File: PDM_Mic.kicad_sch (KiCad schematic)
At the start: 25 parts, among them J4 Conn_FFC_Molex_5019510550, J5 Conn_FFC_Molex_5019510550, U18 TPD4E05U06QDQARQ1, U19 TPD4E05U06QDQARQ1, U20 TLV73318PDBVT, U21 ADAU7118ACPZRL

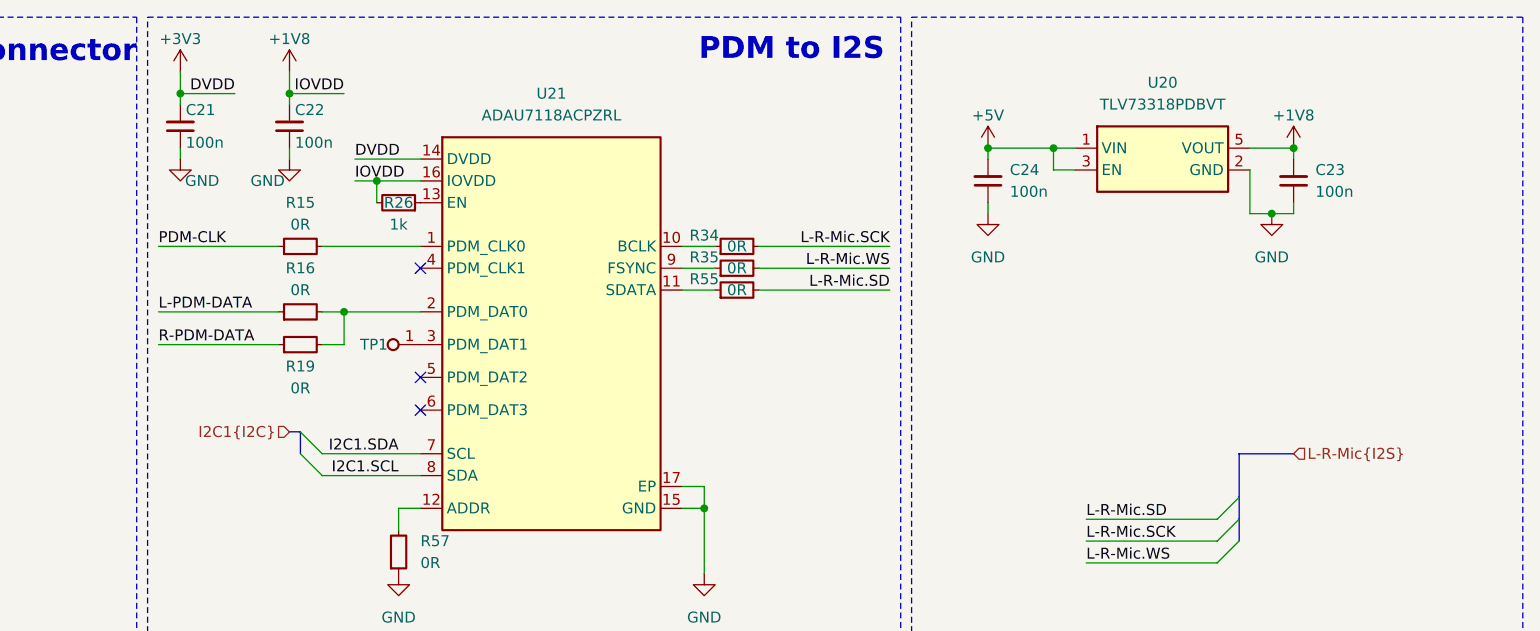
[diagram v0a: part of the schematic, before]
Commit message: [#71230] Route I2S and PDM
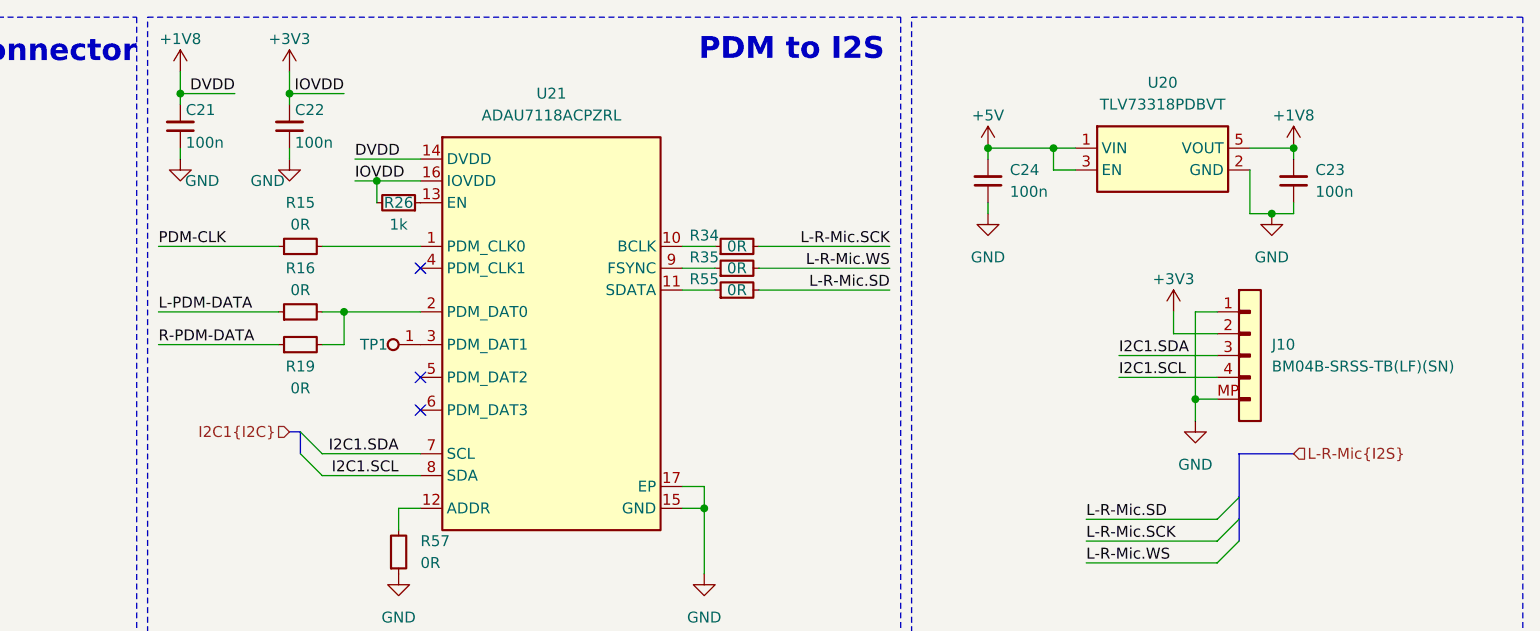
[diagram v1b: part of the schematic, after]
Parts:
- added J10: JST_SH_1x4_BM04B-SRSS-TB-LF-SN, antmicro-footprints:Conn_JST_SH_1x4_BM04B-SRSS-TB-LF-SN, symbol antmicroWire2BoardConnectors:JST_SH_1x4_BM04B-SRSS-TB-LF-SN
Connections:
- net +1V8: now also C21.2, U21.14 (DVDD); no longer C22.2, R26.2, U21.16 (IOVDD)
- net +3V3: now also C22.2, R26.2, U21.16 (IOVDD), J10.2; no longer C21.2, U21.14 (DVDD)
- net GND: now also J10.1, J10.MP
- net I2C1.SCL: now also J10.4
- net I2C1.SDA: now also J10.3

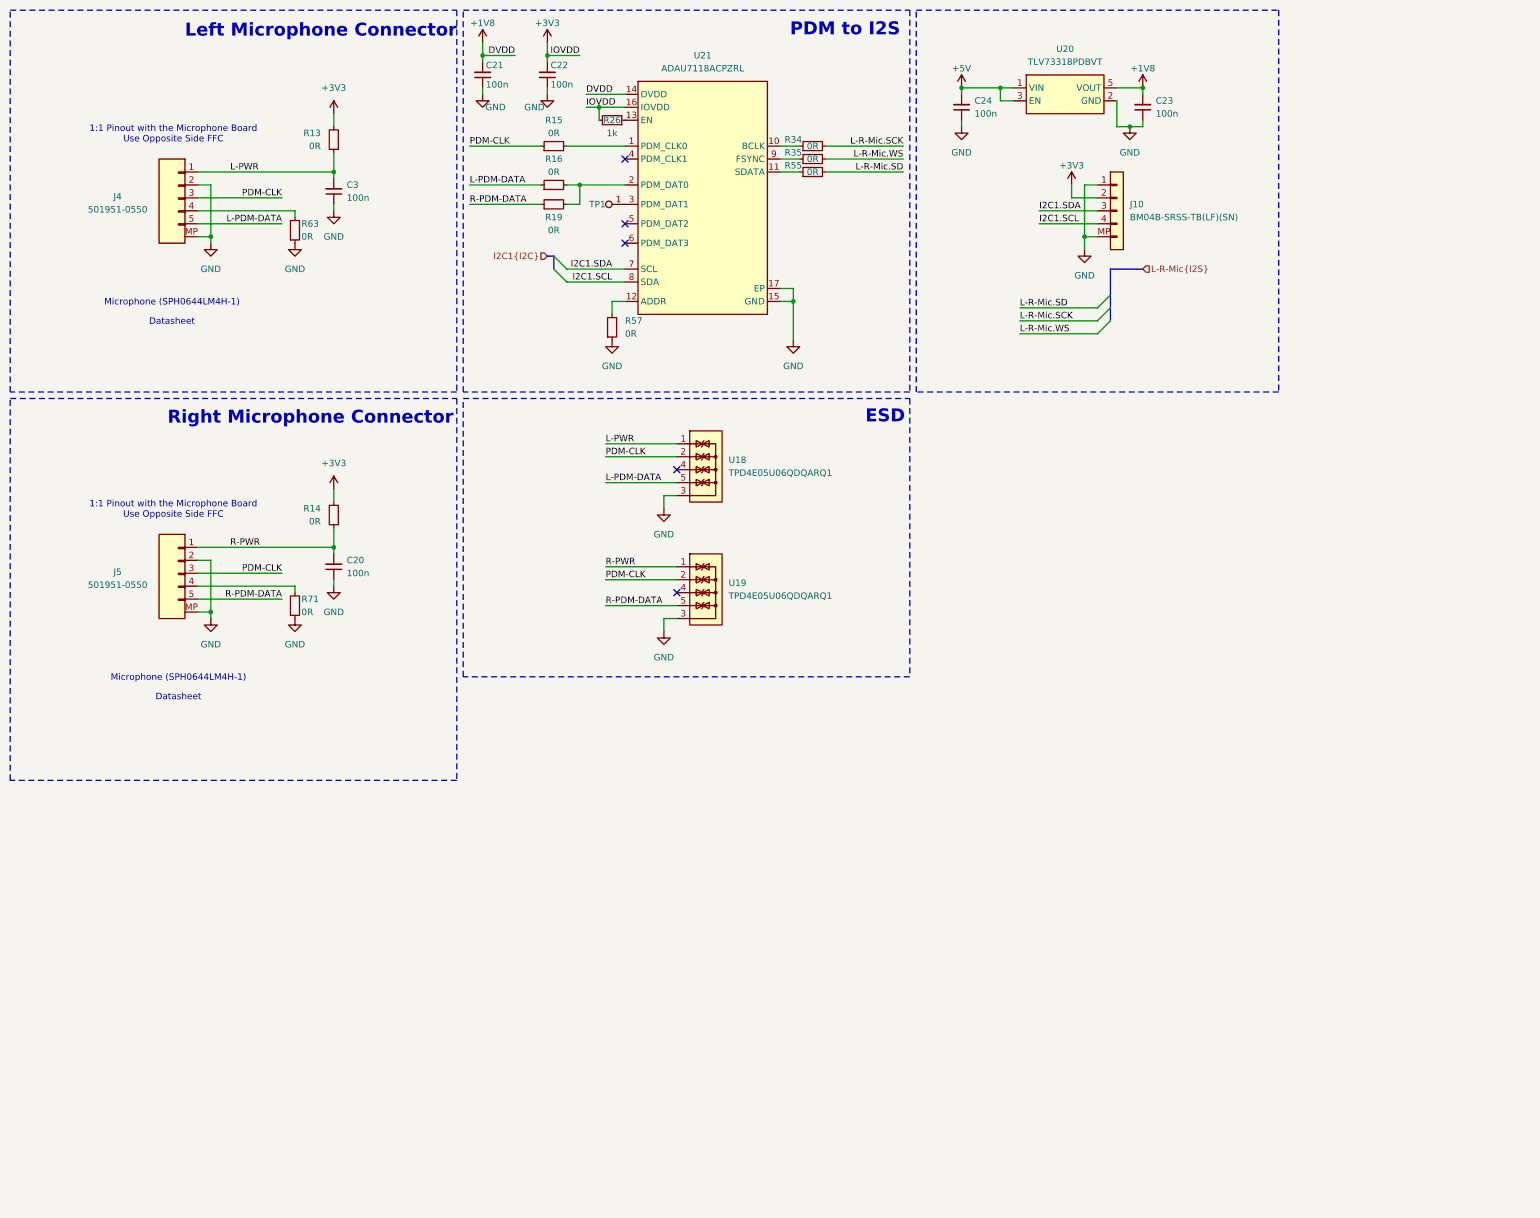
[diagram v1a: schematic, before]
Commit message: [#71230] Add option to connect PDM mic directly to RP2040-0
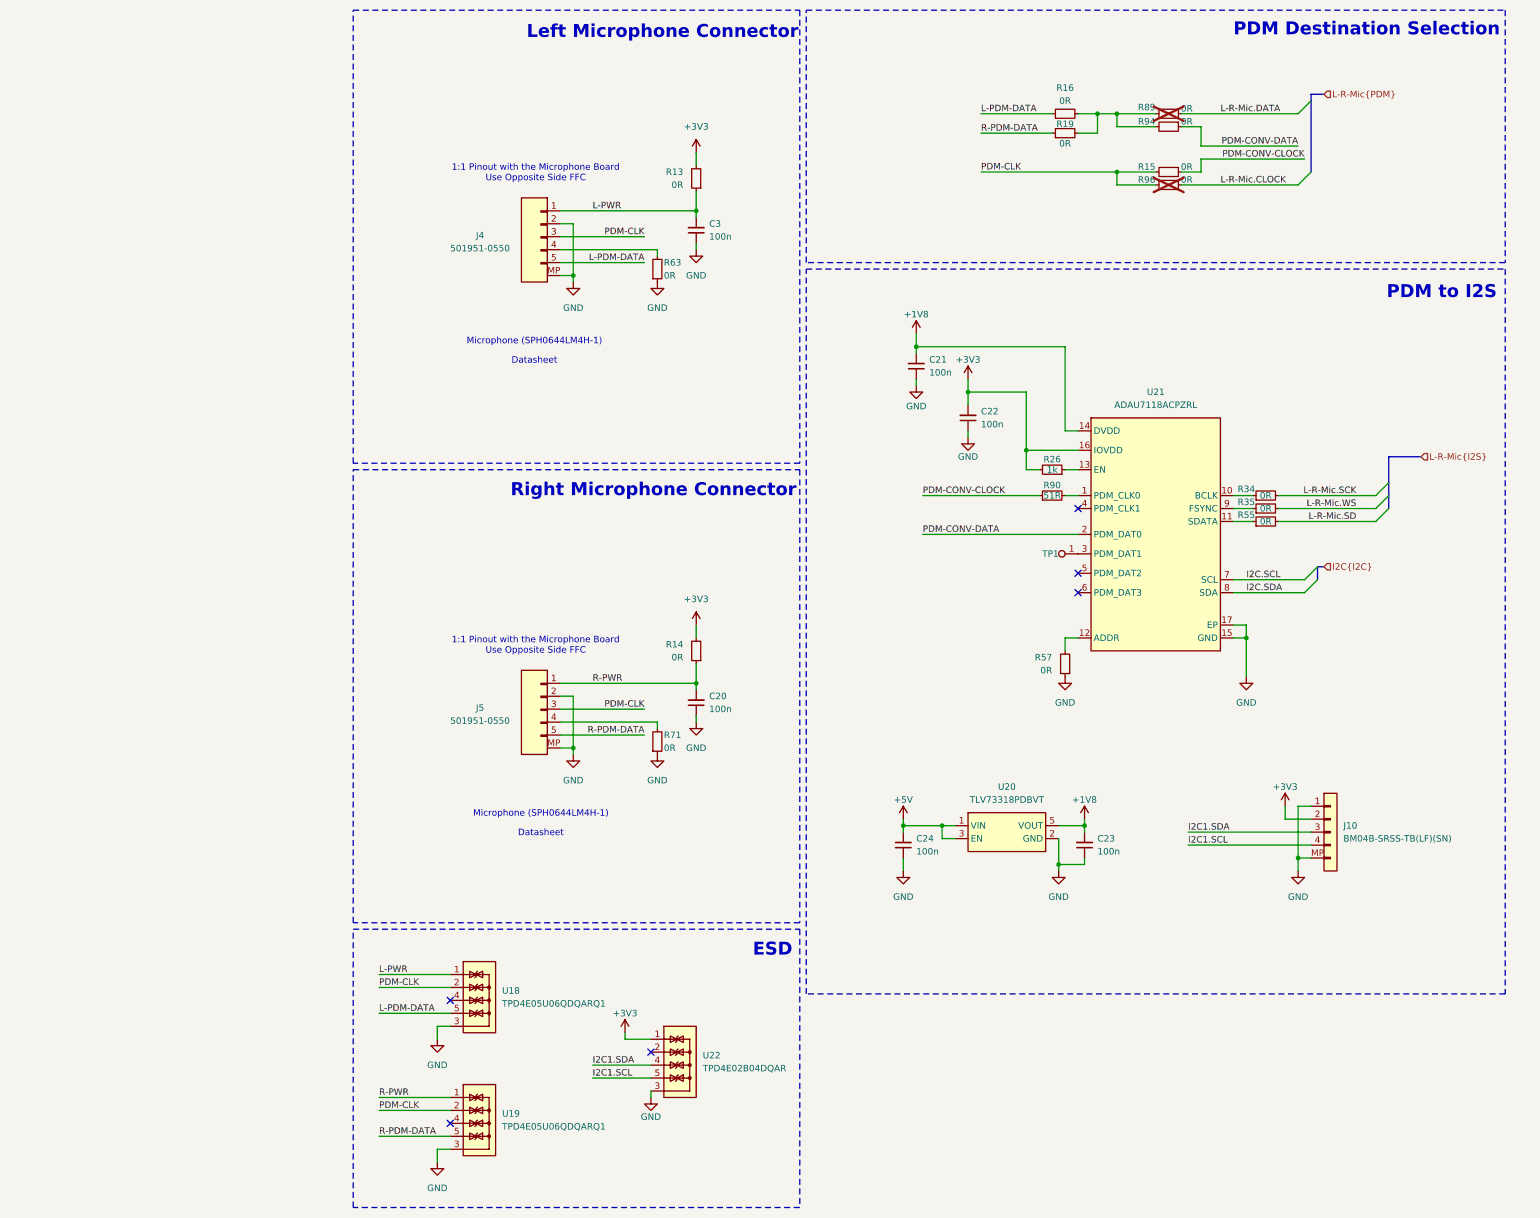
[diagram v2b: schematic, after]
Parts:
- added R89, R94, R96: R_0R_0402, antmicro-footprints:R_0402_1005Metric, symbol antmicroResistors0402:R_0R_0402
- added R90: R_51R_0402, antmicro-footprints:R_0402_1005Metric, symbol antmicroResistors0402:R_51R_0402
- added U22: TPD4E02B04DQA, antmicro-footprints:USON-10_2.5x1mm_P0.5mm, symbol antmicroTVSDiodes:TPD4E02B04DQA
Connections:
- net +3V3: now also U22.1, U22.10
- net GND: now also U22.3, U22.8
- net I2C1.SCL: now also U22.5, U22.6; no longer U21.8 (SDA)
- net I2C1.SDA: now also U22.4, U22.7; no longer U21.7 (SCL)
- net PDM-CLK: now also R15.2, R96.2; no longer R15.1
- net at R16.2, R19.2: now also R89.1, R94.2; no longer U21.2 (PDM_DAT0)
- net at U21.1 (PDM_CLK0): now also R90.2; no longer R15.2
- new net: U22.2, U22.9
- new net I2C.SCL: U21.7 (SCL)
- new net I2C.SDA: U21.8 (SDA)
- new net L-R-Mic.CLOCK: R96.1
- new net L-R-Mic.DATA: R89.2
- new net PDM-CONV-CLOCK: R15.1, R90.1
- new net PDM-CONV-DATA: R94.1, U21.2 (PDM_DAT0)
- no-connect marks 5 -> 6
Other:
- note added: "PDM Destination Selection"
- moved on the sheet: C20, C21, C22, C23, C24, C3, J10, J4, J5, R13, R14, R16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
